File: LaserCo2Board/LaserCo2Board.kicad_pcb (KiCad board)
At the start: 2 copper layers, 131 parts, among them J1 Y VREF, J10 LASER, J11 X MOTOR, J12 Y1 MOTOR, J13 WATER FLOW, J14 Y2 MOTOR, J15 LASER P, J16 X LIMIT1, J17 X LIMIT2, J18 Y LIMIT1, J19 Y LIMIT2, J2 X VREF, J20 D SWITCH, J3 JTAG, J4 USB, J5 POWER IN, J6 FAN1, J7 FAN2, J8 FAN3, J9 PUMP, Q1 BSS138, Q2 BSS138, Q3 BSS138, SW1 SW_PUSH, SW2 SWITCH_INV, U1 STM32F20XR, U2 A4982SLPTR, U3 A4982SLPTR, U4 LD1117S33TR, U5 74HC08A, U6 MCP4725, U7 MCP44X1, U8 74HC1G00, X1 CRYSTAL_4PIN, X2 CRYSTAL

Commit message: First Commit
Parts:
- added ?: , M3, F.Cu at (129.3, 35.5)
- added ?: , M3, F.Cu at (119.3, 63.6)
- added ?: , M3, F.Cu at (55.0, 71.6)
- added ?: , M3, F.Cu at (35.0, 35.0)
- added C39: 100u, C_ELEC_6.3x7.7, F.Cu at (34.8, 55.8)
- moved J6 37.5 mm to (34.5, 71.2)
- moved J9 3.00 mm to (34.5, 78.2), turned to 0 degrees
- moved J11 0.16 mm to (71.1, 33.8)
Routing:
- net GND: track 13.3 -> 782.3 mm, vias 0 -> 384
- net +3.3V: track 347.8 -> 522.2 mm, vias 21 -> 44
- net X_LIMIT1: track 9.44 -> 105.9 mm, vias 0 -> 6
- net Y_EN: track 0.00 -> 95.4 mm, vias 0 -> 4
- net WATER_FLOW: track 0.00 -> 85.6 mm, vias 0 -> 2
- net Y_LIMIT1: track 9.44 -> 94.8 mm, vias 0 -> 2
- net Y_DIR: track 0.00 -> 84.6 mm, vias 0 -> 4
- net LASER_POINT: track 1.76 -> 85.5 mm, vias 0 -> 2
- net X_LIMIT2: track 9.44 -> 81.2 mm, vias 0 -> 6
- net SCL1: track 1.76 -> 71.2 mm, vias 0 -> 2
- net SDA1: track 1.76 -> 66.7 mm, vias 0 -> 2
- net LASER_OUT: track 5.50 -> 70.0 mm, vias 0 -> 2
- net Y_STEP: track 0.00 -> 64.3 mm, vias 0 -> 2
- net X_EN: track 0.00 -> 53.7 mm, vias 0 -> 4
- net Y_LIMIT2: track 9.44 -> 62.5 mm, vias 0 -> 6
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- added copper zone on B.Cu, net +3.3V
- added copper zone on F.Cu, net +3.3V
- added copper zone on B.Cu, net GND
- added copper zone on F.Cu, net GND
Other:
- board outline added: 106.8 x 52.5 mm
- net class Default: clearance 0.1524 -> 0.127; trace_width 0.381 -> 0.254; via_dia 0.59944 -> 0.50038; via_drill 0.39878 -> 0.33528
- rule trace_clearance: 0.1524 -> 0.127

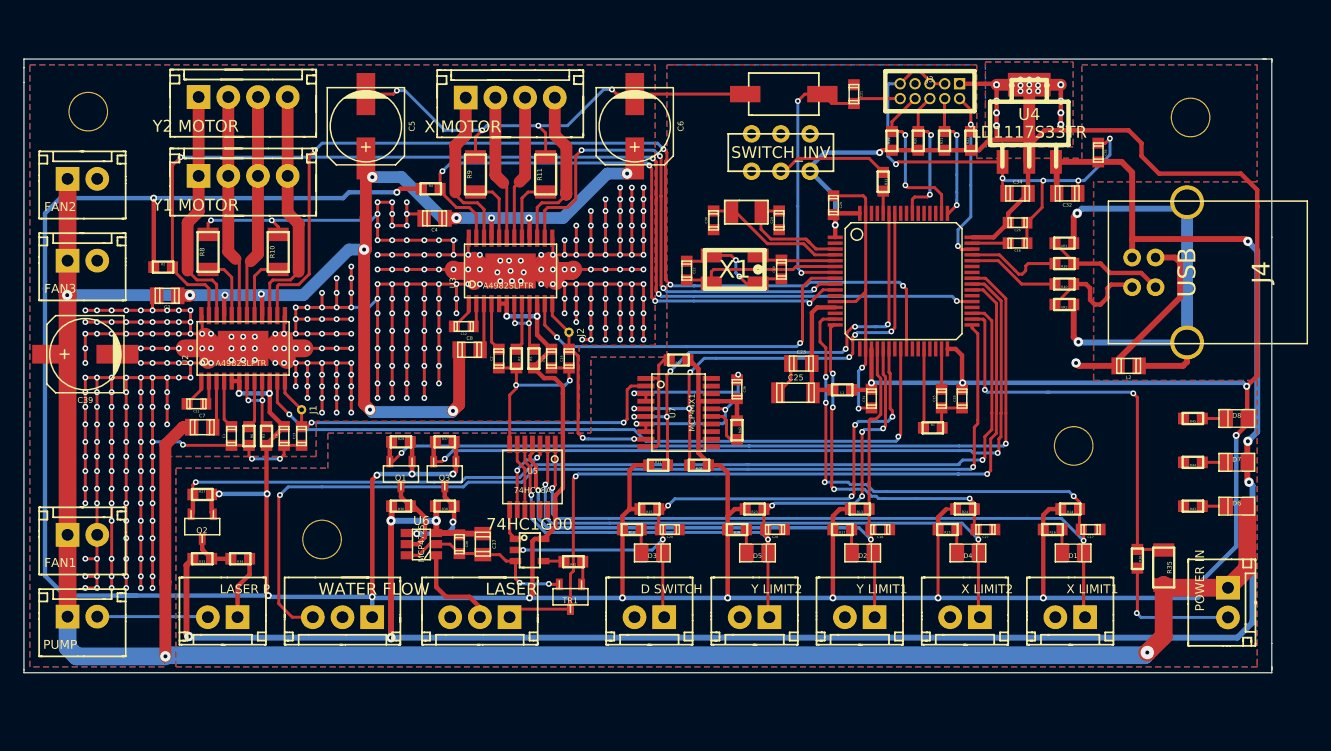
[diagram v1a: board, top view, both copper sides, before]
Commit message: サンプル確認後の修正
#16
#15
#14
#13
#12
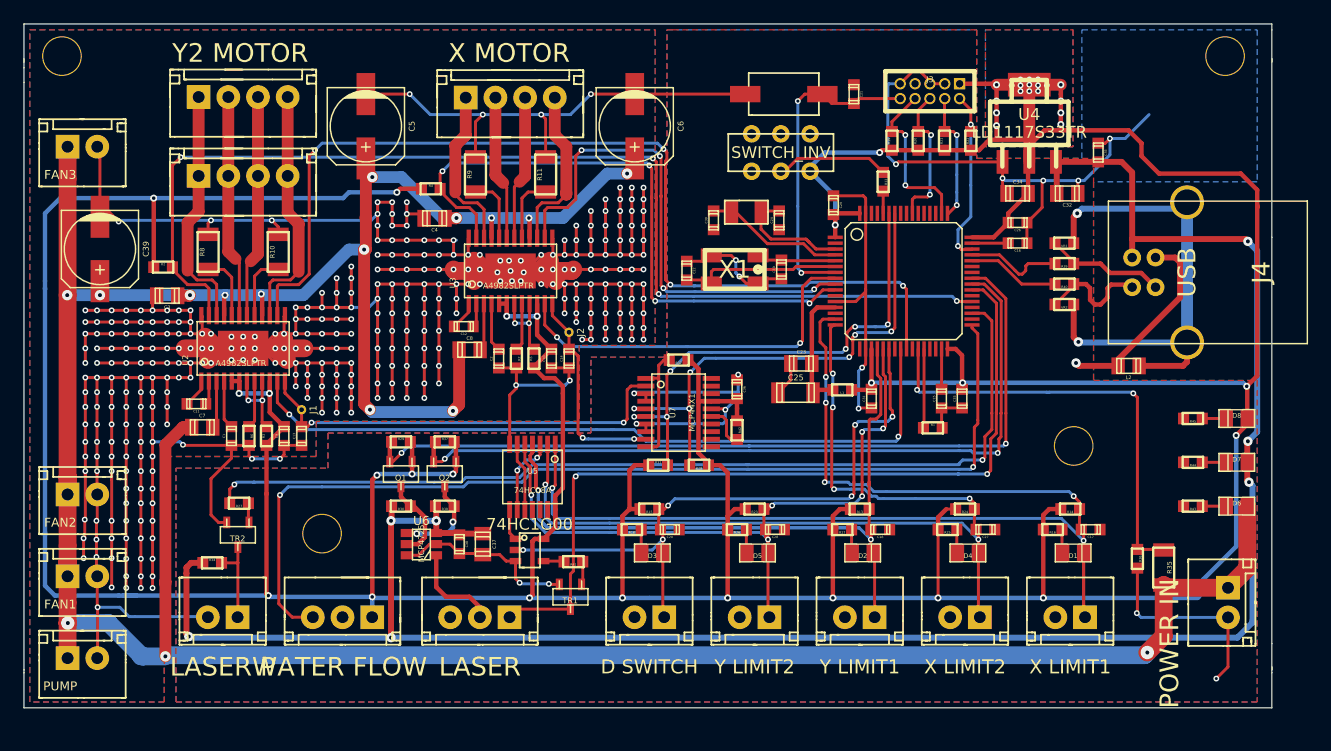
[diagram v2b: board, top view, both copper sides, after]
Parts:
- removed Q3: BSS138, SOT-23
- removed R33: 10k, R_0603
- added TR2: BSH105, SOT-23, F.Cu at (47.8, 71.2)
- R27: value 10k -> 100R
- R34: value 75R -> 22R
- R44: value 1K -> 1k5
- moved J7 27.0 mm to (34.5, 67.8)
- moved Q2 21.2 mm to (65.5, 66.0)
- moved J8 9.75 mm to (34.5, 38.0)
- moved C39 9.09 mm to (36.0, 46.8), turned to 270 degrees
- moved ? 6.02 mm to (132.2, 30.2)
- moved ? 5.26 mm to (32.8, 30.2)
- moved J6 3.55 mm to (34.5, 74.8)
- moved J9 3.55 mm to (34.5, 81.8)
- moved R27 3.24 mm to (47.9, 68.5), turned to 180 degrees
- moved R34 2.43 mm to (45.6, 73.6), turned to 0 degrees
- moved ? 0.50 mm to (55.0, 71.1)
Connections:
- Q2 pad D: N-0000050 (its old number) -> N-0000071
- Q2 pad S: LASER_POINT -> SDA1
- R27 pad 1: LASER_POINT -> N-0000036
- R27 pad 2: +3.3V -> LASER_POINT
- R34 pad 1: LASER_POINT_CONN -> VBUS
- R34 pad 2: N-0000050 (its old number) -> LASER_POINT_CONN
- R38 pad 1: N-0000064 -> N-0000071
- U1 pad 27: (no net) -> CHECK_12V
- U1 pad 34: CHECK_12V -> (no net)
- U6 pad 4: N-0000064 -> N-0000071
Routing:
- net GND: track 782.3 -> 833.3 mm, vias 384 -> 386
- net N-0000071: track 0.00 -> 8.12 mm, vias 0 -> 2
- net N-0000064: track 8.12 -> 0.00 mm, vias 2 -> 0
- net V_IN: track 291.8 -> 284.8 mm, vias 14 -> 16
- net +3.3V: track 522.2 -> 516.0 mm, vias 44 -> 42
- net LASER_POINT: track 85.5 -> 81.2 mm
- net N-0000050 (its old number): track 3.67 -> 0.00 mm
- net CHECK_12V: track 35.9 -> 37.9 mm
- net LASER_POINT_CONN: track 5.43 -> 7.41 mm
- net N-0000036: track 0.00 -> 1.67 mm
- net VBUS: track 190.9 -> 191.5 mm
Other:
- board size 106.8 x 52.5 mm -> 106.8 x 58.5 mm

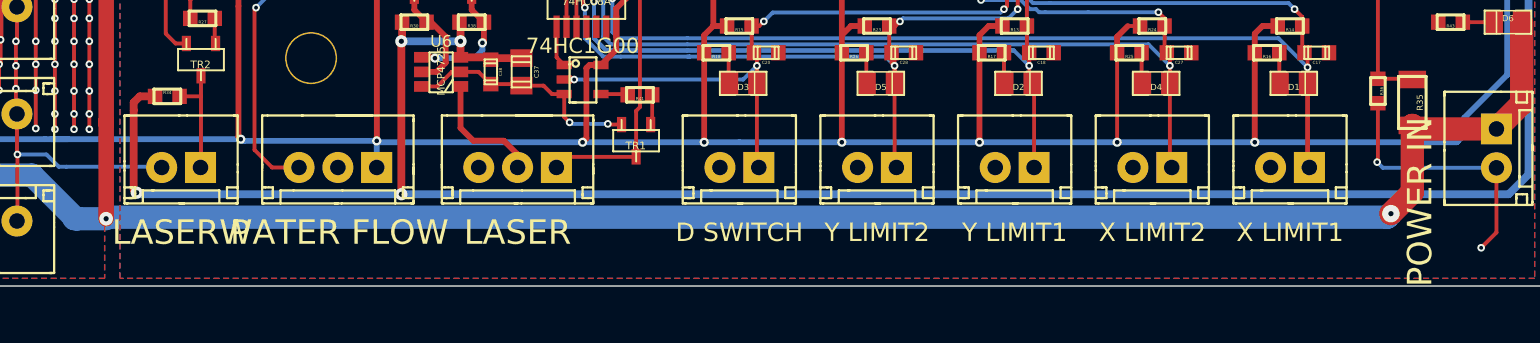
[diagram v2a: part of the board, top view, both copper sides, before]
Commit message: シルク文字修正
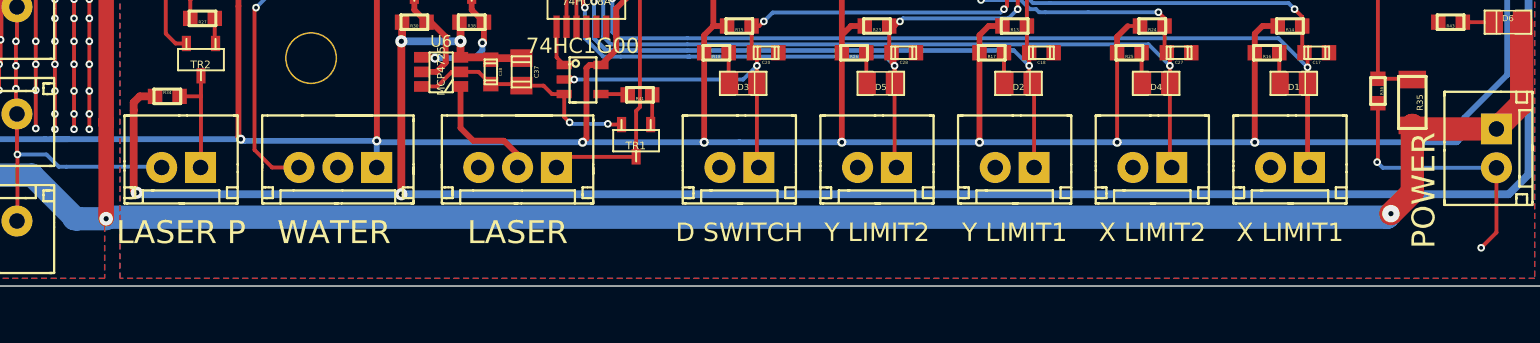
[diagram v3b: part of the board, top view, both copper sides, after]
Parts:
- J13: value WATER FLOW -> WATER
- J5: value POWER IN -> POWER
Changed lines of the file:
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@@
     (links 313)
     (no_connects 0)
-    (area 29.449999 27.449999 136.300001 86.050001)
+    (area 29.449999 27.449999 139.604501 88.015111)
     (thickness 1.6)
     (drawings 16)
@@
       (effects (font (size 1.016 1.016) (thickness 0.1524)))
     )
-    (fp_text value "WATER FLOW" (at 0.25 -4.25 180) (layer F.SilkS)
-      (effects (font (size 1.6 1.6) (thickness 0.3)))
+    (fp_text value WATER (at 0.25 -4.25 180) (layer F.SilkS)
+      (effects (font (size 1.5 1.5) (thickness 0.3)))
     )
     (fp_line (start 4.25 -1.8) (end 4.25 -1.5) (layer F.SilkS) (width 0.15))
@@
     )
     (fp_text value LASER (at 0 -4.25 180) (layer F.SilkS)
-      (effects (font (size 1.6 1.6) (thickness 0.3)))
+      (effects (font (size 1.5 1.5) (thickness 0.3)))
     )
     (fp_line (start 4.25 -1.8) (end 4.25 -1.5) (layer F.SilkS) (width 0.15))
@@
       (effects (font (size 0.762 0.762) (thickness 0.1524)))
     )
-    (fp_text value "POWER IN" (at 3.5 5 270) (layer F.SilkS)
-      (effects (font (size 1.6 1.6) (thickness 0.3)))
+    (fp_text value POWER (at 2.75 4.75 270) (layer F.SilkS)
+      (effects (font (size 1.5 1.5) (thickness 0.3)))
     )
     (fp_line (start 3 -1.7) (end 3 -2) (layer F.SilkS) (width 0.15))
@@
     )
     (fp_text value "LASER P" (at 0 -4.25 180) (layer F.SilkS)
-      (effects (font (size 1.6 1.6) (thickness 0.3)))
+      (effects (font (size 1.5 1.5) (thickness 0.3)))
     )
     (fp_line (start 3 -1.7) (end 3 -2) (layer F.SilkS) (width 0.15))

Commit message: 変更
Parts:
- removed R27: 100R, R_0603
- removed TR2: BSH105, SOT-23
- J13: value WATER -> WATER FLOW
- J5: value POWER -> POWER IN
- R34: value 22R -> 47R
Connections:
- net LASER_POINT_CONN renamed N-0000065
- U1 pad 35: LASER_POINT -> (no net)
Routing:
- net LASER_POINT: track 81.2 -> 0.00 mm, vias 2 -> 0
- net GND: track 833.3 -> 825.1 mm
- net N-0000036: track 1.67 -> 0.00 mm
- net N-0000065: track 7.41 -> 6.06 mm

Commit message: ノイズ対策
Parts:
- added C40: 0u1, C_0603, F.Cu at (105.5, 59.5)
- added L3: BLM21SN300SN1D, C_0805, F.Cu at (132.9, 77.8)
- added L4: BLM21SN300SN1D, C_0805, F.Cu at (130.3, 77.8)
- added R27: 22R, R_0603, F.Cu at (75.6, 79.3)
- moved C39 97.2 mm to (130.1, 71.0), turned to 0 degrees
- moved R36 10.3 mm to (124.5, 63.0)
- moved R35 10.2 mm to (126.5, 63.8)
- moved J5 6.36 mm to (131.6, 83.3), turned to 180 degrees
- moved D6 3.45 mm to (133.1, 65.3)
- moved R43 3.45 mm to (129.6, 65.3)
- moved D7 2.40 mm to (133.1, 62.6)
- moved R44 2.40 mm to (129.6, 62.6)
- moved D8 1.36 mm to (133.1, 59.9)
- moved R45 1.35 mm to (129.5, 59.9)
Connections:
- J10 pad 1: LASER_OUT -> LASER_OUT_CONN
- J5 pad 1: V_IN -> N-0000036
- J5 pad 2: GND -> N-0000035
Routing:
- net GND: track 825.1 -> 842.4 mm, vias 386 -> 390
- net V_IN: track 284.8 -> 299.0 mm, vias 16 -> 15
- net CHECK_12V: track 37.9 -> 29.3 mm, vias 2 -> 4
- net +3.3V: track 516.0 -> 509.1 mm, vias 42 -> 43
- net N-0000036: track 0.00 -> 4.61 mm
- net N-0000035: track 0.00 -> 4.61 mm
- net LASER_OUT_CONN: track 0.00 -> 4.19 mm
- net LASER_OUT: track 70.0 -> 66.4 mm
- net VBUS: track 191.5 -> 190.0 mm, vias 7 -> 9

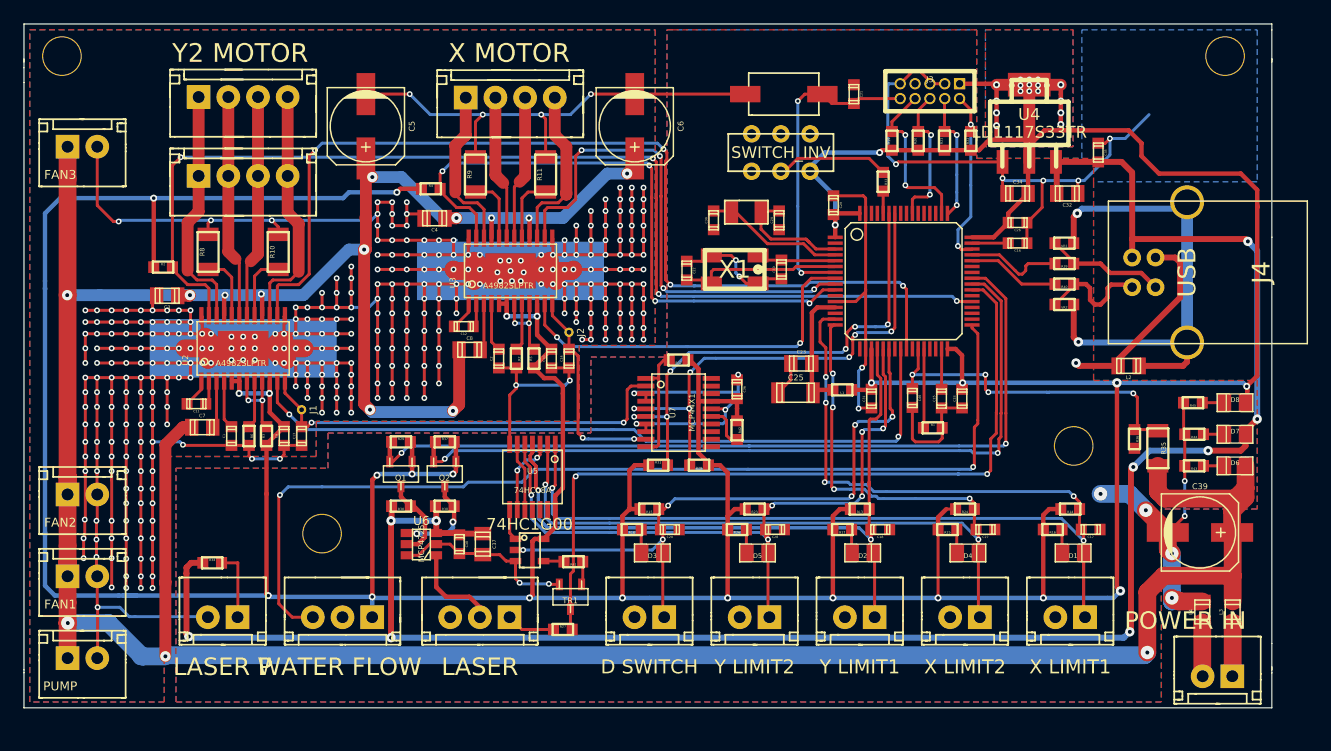
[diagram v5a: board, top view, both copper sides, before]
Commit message: 穴位置を0.5移動
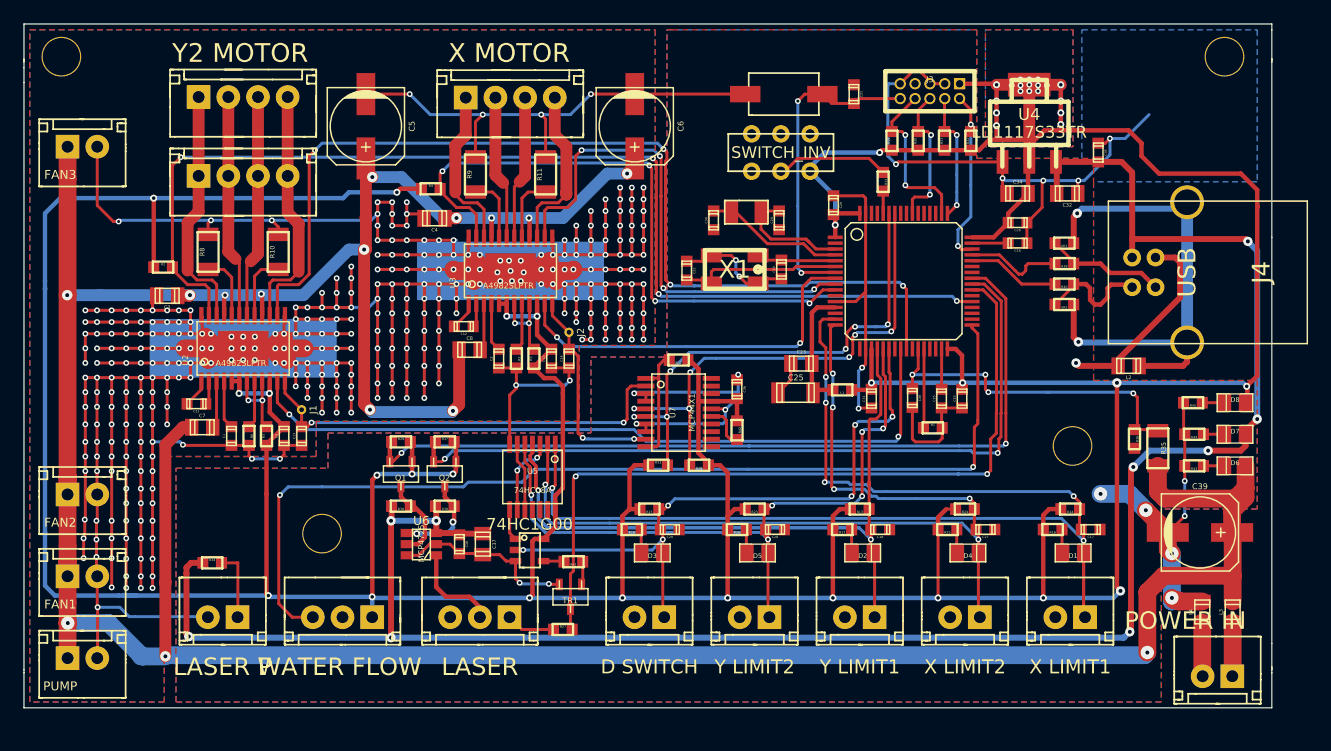
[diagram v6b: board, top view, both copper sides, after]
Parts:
- moved ? 0.10 mm to (119.2, 63.6)
- moved ? 0.07 mm to (132.2, 30.3)
- moved ? 0.07 mm to (32.7, 30.3)
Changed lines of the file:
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@@
   )
   (module M3 (layer F.Cu)
-    (at 132.25 30.25)
+    (at 132.2 30.3)
     (fp_text reference "" (at 0 0) (layer F.SilkS) hide
       (effects (font (size 1 1) (thickness 0.15)))
@@
   )
   (module M3 (layer F.Cu)
-    (at 119.3 63.6)
+    (at 119.2 63.6)
     (fp_text reference "" (at 0 0) (layer F.SilkS) hide
       (effects (font (size 1 1) (thickness 0.15)))
@@
   )
   (module M3 (layer F.Cu)
-    (at 32.75 30.25)
+    (at 32.7 30.3)
     (fp_text reference "" (at 0 0) (layer F.SilkS) hide
       (effects (font (size 1 1) (thickness 0.15)))
